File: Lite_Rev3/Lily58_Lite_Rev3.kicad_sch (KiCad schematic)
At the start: 118 parts, among them J1 M2HOLE, J10 LOGO, J10 M2HOLE, J11 LOGO, J11 M2HOLE, J12 HOLE, J13 HOLE, J14 HOLE, J15 HOLE, J16 OLED_R, J19 breakaway, J2 M2HOLE, J20 breakaway, J21 breakaway, J22 AudioJack4, J22 breakaway, J3 HOLE, J4 HOLE, J5 HOLE, J6 HOLE, J7 OLED_L, J9 AudioJack4, SW1 SW_Push, SW10 SW_Push, SW11 SW_Push, SW12 SW_Push, SW13 SW_Push, SW14 SW_Push, SW15 SW_Push, SW16 SW_Push, SW17 SW_Push, SW18 SW_Push, SW19 SW_Push, SW2 SW_Push, SW20 SW_Push, SW21 SW_Push, SW22 SW_Push, SW23 SW_Push, SW24 SW_Push, SW25 SW_Push, SW26 SW_Push, SW27 SW_Push, SW28 SW_Push, SW29 SW_Push, SW3 SW_Push, SW30 SW_Push, SW31 SW_Push, SW32 SW_Push, SW33 SW_Push, SW34 SW_Push, SW35 SW_Push, SW36 SW_Push, SW37 SW_Push, SW38 SW_Push, SW39 SW_Push, SW4 SW_Push, SW40 SW_Push, SW41 SW_Push, SW42 SW_Push, SW43 SW_Push, SW44 SW_Push, SW45 SW_Push, SW46 SW_Push, SW47 SW_Push, SW48 SW_Push, SW49 SW_Push, SW5 SW_Push, SW50 SW_Push, SW51 SW_Push, SW52 SW_Push, SW53 SW_Push, SW54 SW_Push, SW55 SW_Push, SW56 SW_Push, SW57 SW_Push, SW58 SW_Push, SW6 SW_Push, SW7 SW_Push, SW8 SW_Push, SW9 SW_Push

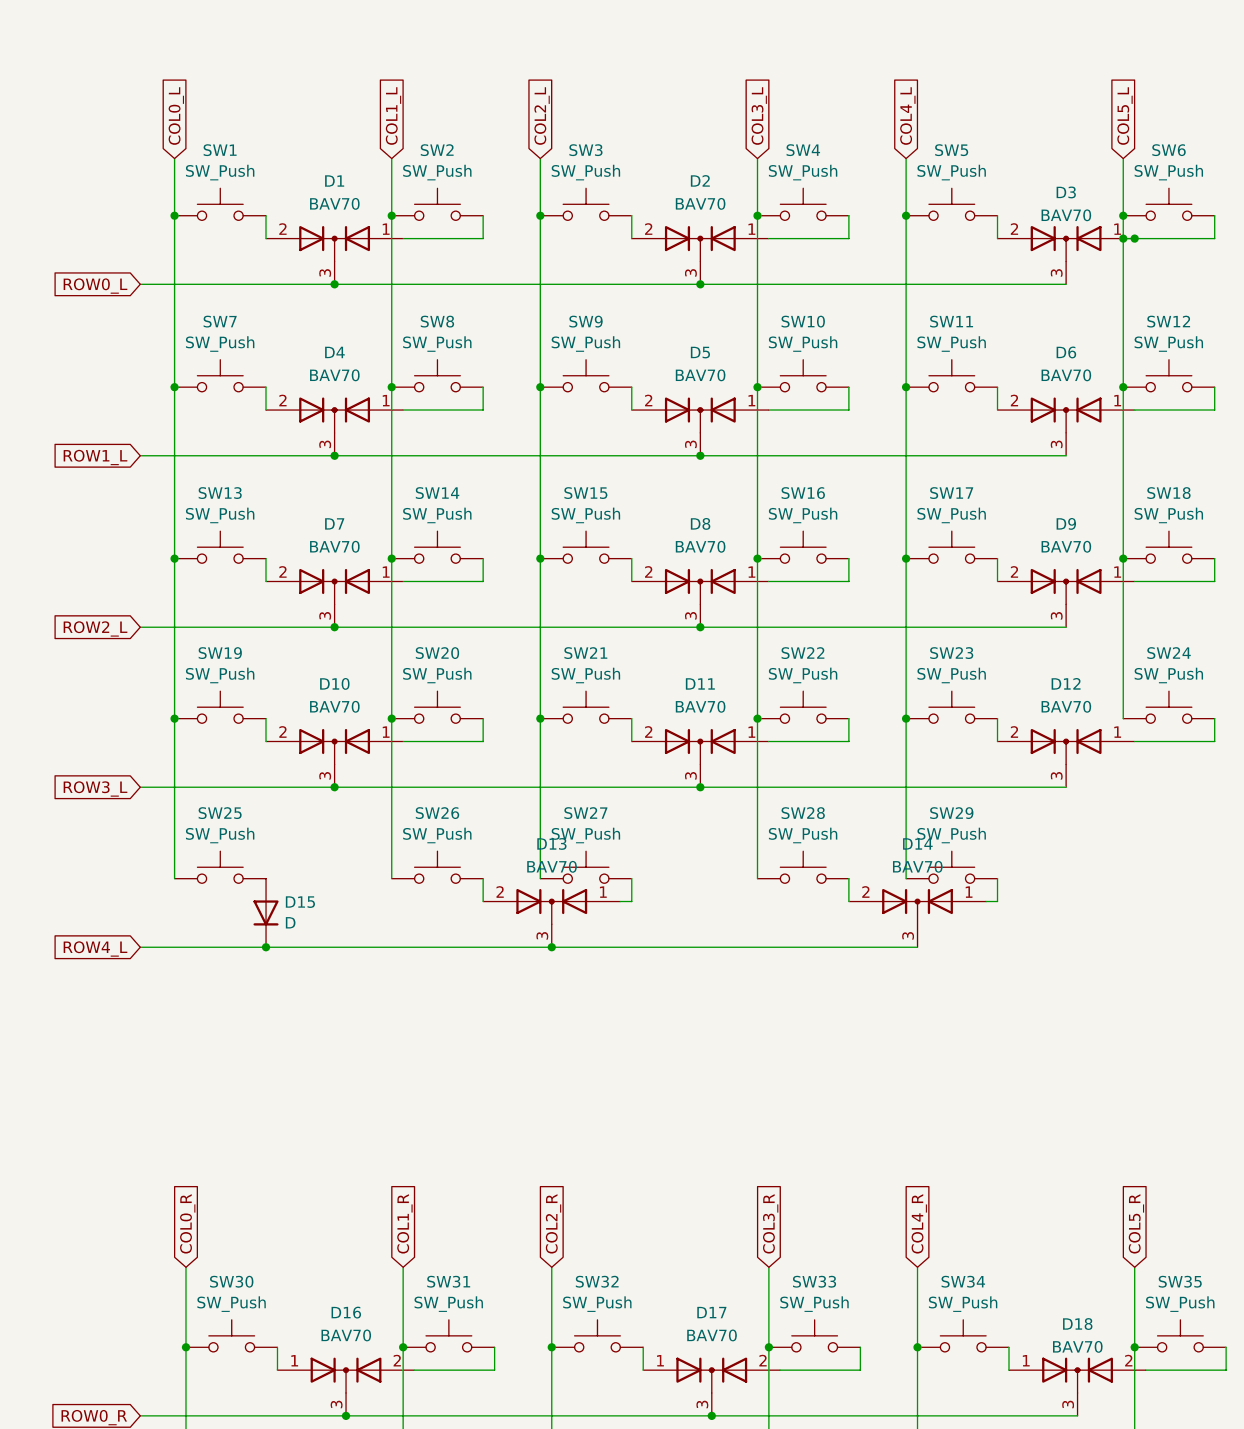
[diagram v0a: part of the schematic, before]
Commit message: [Lily58 Lite Rev3] fix cols pin
Changed to the same cols pin as Lily58 Pro and Lily58 Pro v2
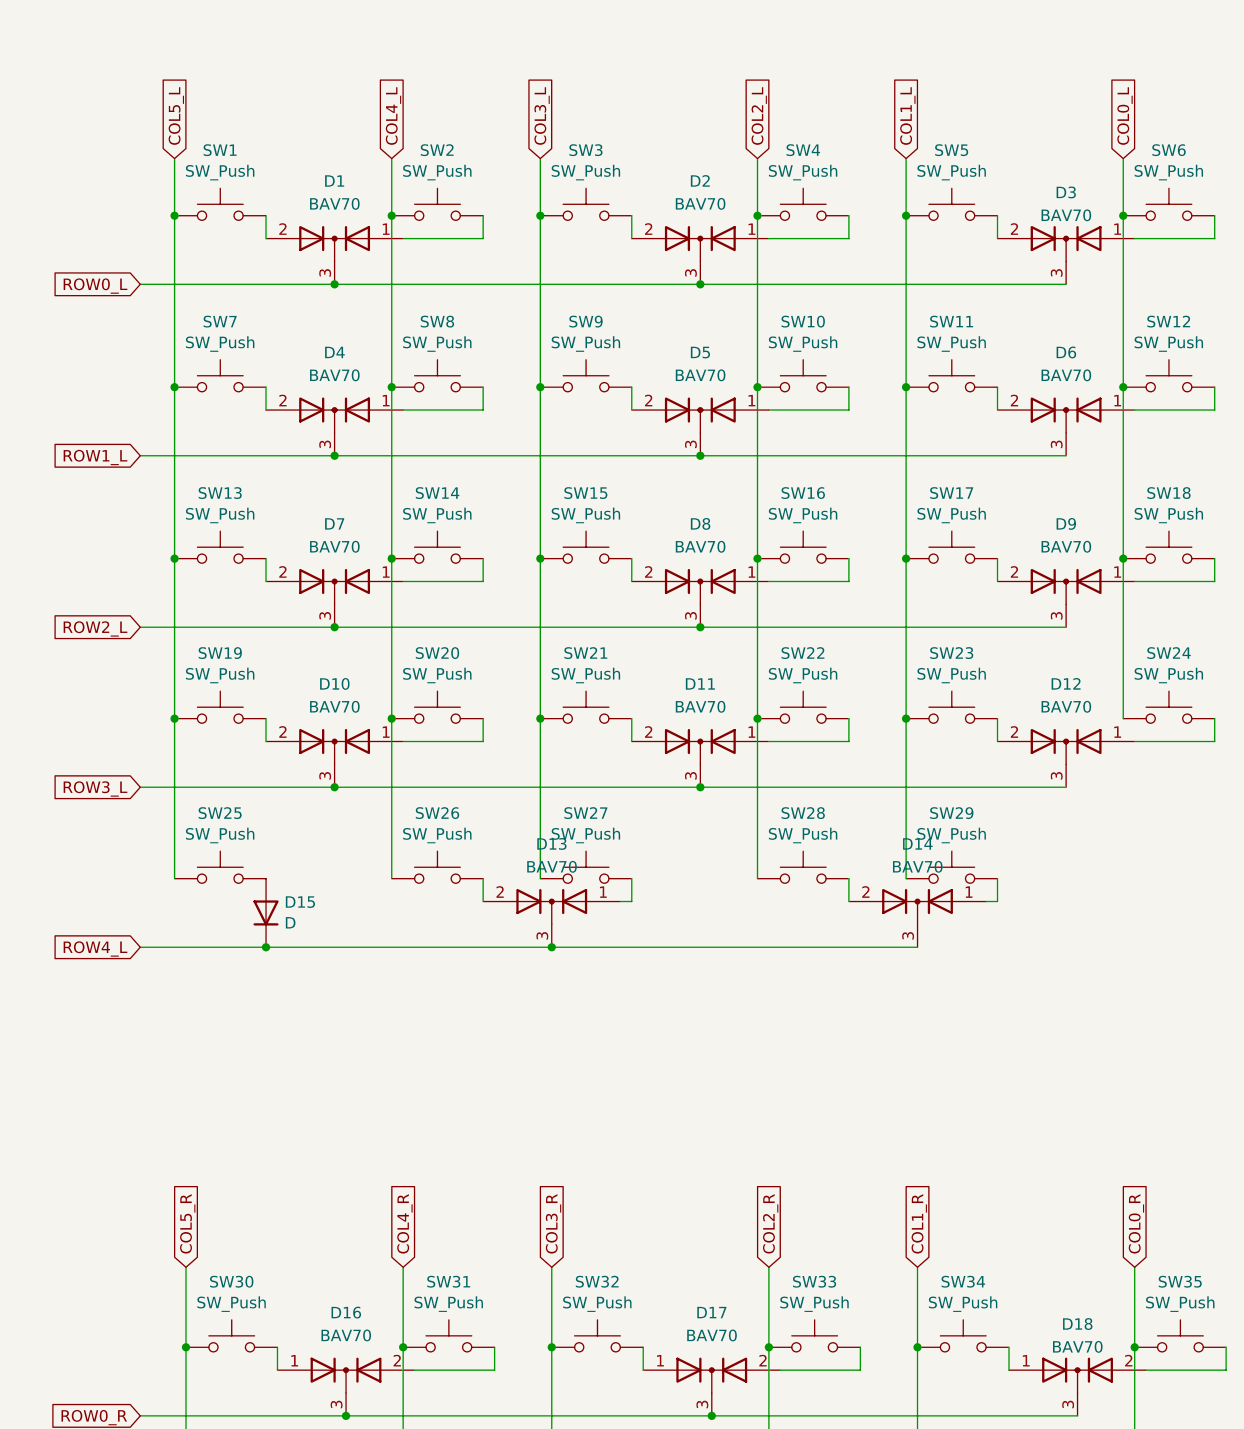
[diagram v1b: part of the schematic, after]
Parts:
- SW1, SW10, SW11, SW12, SW13, SW14, SW15, SW16, SW17, SW18, SW19, SW2, SW20, SW21, SW22, SW23, SW24, SW25, SW26, SW27, SW28, SW29, SW3, SW30, SW31, SW32, SW33, SW34, SW35, SW36, SW37, SW38, SW39, SW4, SW40, SW41, SW42, SW43, SW44, SW45, SW46, SW47, SW48, SW49, SW5, SW50, SW51, SW52, SW53, SW54, SW55, SW56, SW57, SW58, SW6, SW7, SW8, SW9: footprint yuchi_kbd:MX_HOLE -> yuchi:MX_HOLE_FB-SIlk
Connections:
- net COL0_L: now also SW12.1, SW18.1, SW24.1, SW6.1; no longer SW1.1, SW13.1, SW19.1, SW25.1, SW7.1
- net COL0_R: now also SW35.1, SW41.1, SW47.1, SW53.1; no longer SW30.1, SW36.1, SW42.1, SW48.1, SW54.1
- net COL1_L: now also SW11.1, SW17.1, SW23.1, SW29.1, SW5.1; no longer SW14.1, SW2.1, SW20.1, SW26.1, SW8.1
- net COL1_R: now also SW34.1, SW40.1, SW46.1, SW52.1, SW58.1; no longer SW31.1, SW37.1, SW43.1, SW49.1, SW55.1
- net COL2_L: now also SW10.1, SW16.1, SW22.1, SW28.1, SW4.1; no longer SW15.1, SW21.1, SW27.1, SW3.1, SW9.1
- net COL2_R: now also SW33.1, SW39.1, SW45.1, SW51.1, SW57.1; no longer SW32.1, SW38.1, SW44.1, SW50.1, SW56.1
- net COL3_L: now also SW15.1, SW21.1, SW27.1, SW3.1, SW9.1; no longer SW10.1, SW16.1, SW22.1, SW28.1, SW4.1
- net COL3_R: now also SW32.1, SW38.1, SW44.1, SW50.1, SW56.1; no longer SW33.1, SW39.1, SW45.1, SW51.1, SW57.1
- net COL4_L: now also SW14.1, SW2.1, SW20.1, SW26.1, SW8.1; no longer SW11.1, SW17.1, SW23.1, SW29.1, SW5.1
- net COL4_R: now also SW31.1, SW37.1, SW43.1, SW49.1, SW55.1; no longer SW34.1, SW40.1, SW46.1, SW52.1, SW58.1
- net COL5_L: now also SW1.1, SW13.1, SW19.1, SW25.1, SW7.1; no longer D3.1 (A), SW12.1, SW18.1, SW24.1, SW6.1, SW6.2
- net COL5_R: now also SW30.1, SW36.1, SW42.1, SW48.1, SW54.1; no longer SW35.1, SW41.1, SW47.1, SW53.1
- new net: D3.1 (A), SW6.2

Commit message: [Lily58 Lite Rev3] Fix SW54
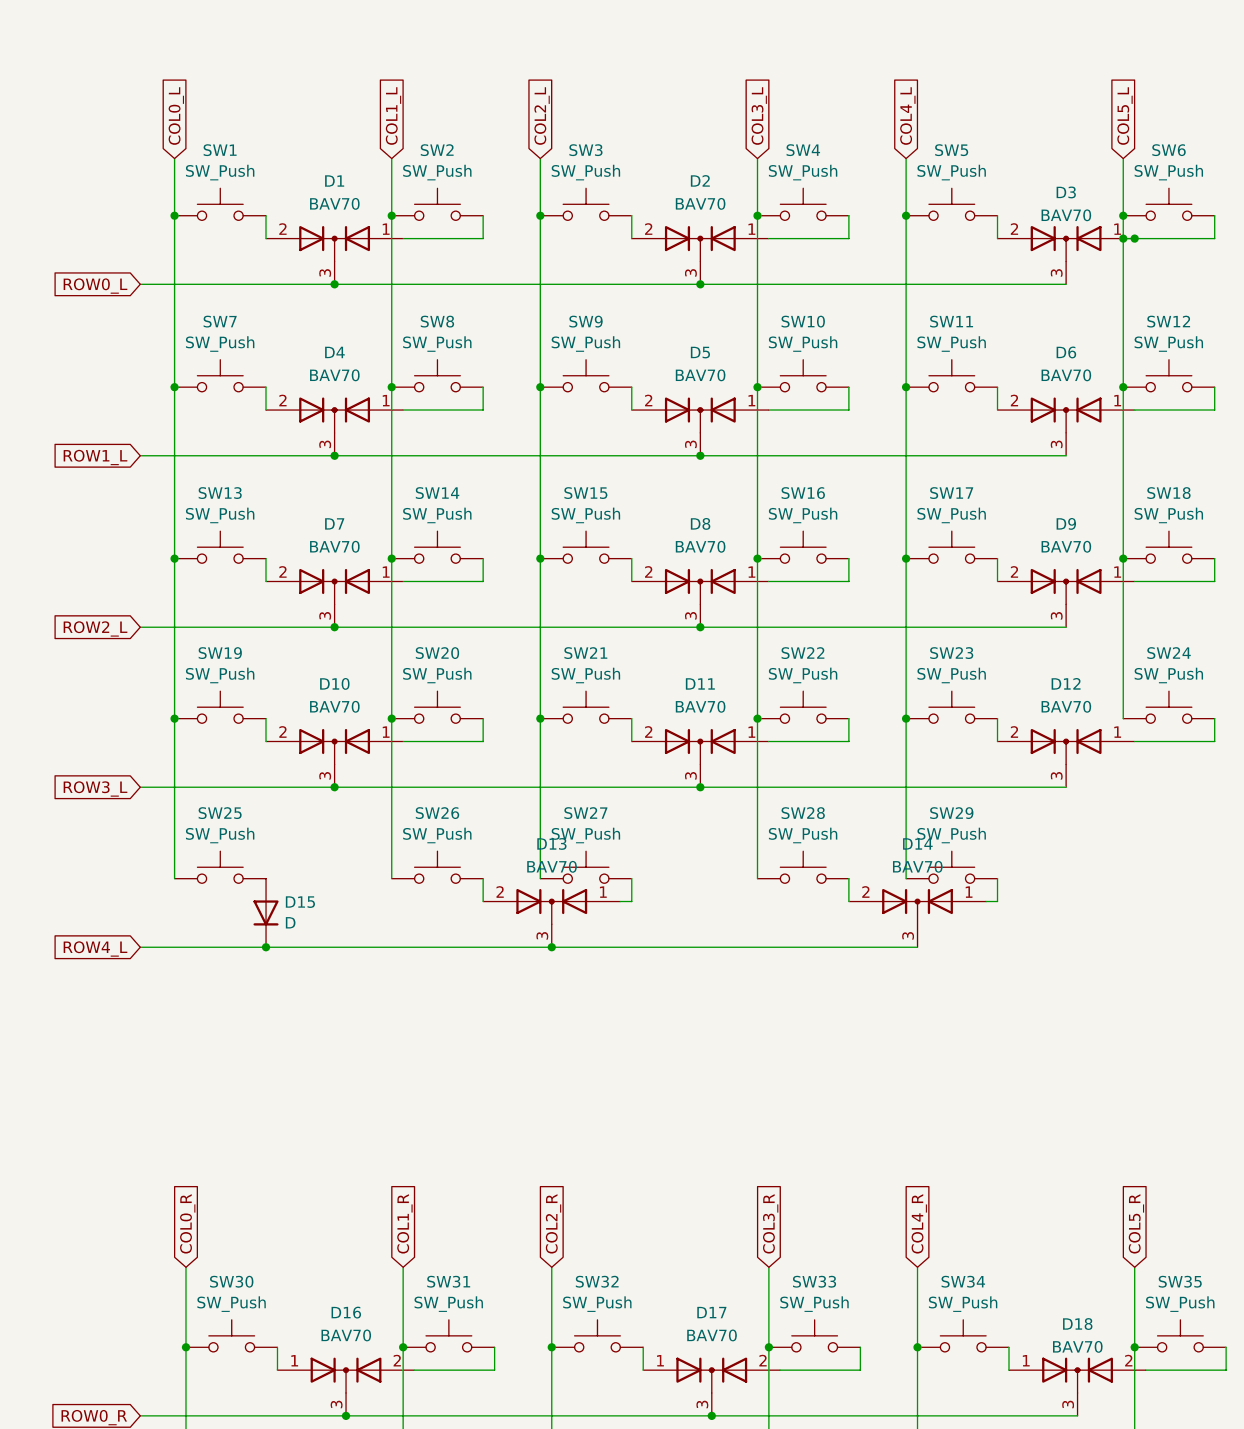
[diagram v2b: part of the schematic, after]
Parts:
- SW1, SW10, SW11, SW12, SW13, SW14, SW15, SW16, SW17, SW18, SW19, SW2, SW20, SW21, SW22, SW23, SW24, SW25, SW26, SW27, SW28, SW29, SW3, SW30, SW31, SW32, SW33, SW34, SW35, SW36, SW37, SW38, SW39, SW4, SW40, SW41, SW42, SW43, SW44, SW45, SW46, SW47, SW48, SW49, SW5, SW50, SW51, SW52, SW53, SW54, SW55, SW56, SW57, SW58, SW6, SW7, SW8, SW9: footprint yuchi:MX_HOLE_FB-SIlk -> yuchi_kbd:MX_HOLE
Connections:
- net COL0_L: now also SW1.1, SW13.1, SW19.1, SW25.1, SW7.1; no longer SW12.1, SW18.1, SW24.1, SW6.1
- net COL0_R: now also SW30.1, SW36.1, SW42.1, SW48.1, SW54.1; no longer SW35.1, SW41.1, SW47.1, SW53.1
- net COL1_L: now also SW14.1, SW2.1, SW20.1, SW26.1, SW8.1; no longer SW11.1, SW17.1, SW23.1, SW29.1, SW5.1
- net COL1_R: now also SW31.1, SW37.1, SW43.1, SW49.1, SW55.1; no longer SW34.1, SW40.1, SW46.1, SW52.1, SW58.1
- net COL2_L: now also SW15.1, SW21.1, SW27.1, SW3.1, SW9.1; no longer SW10.1, SW16.1, SW22.1, SW28.1, SW4.1
- net COL2_R: now also SW32.1, SW38.1, SW44.1, SW50.1, SW56.1; no longer SW33.1, SW39.1, SW45.1, SW51.1, SW57.1
- net COL3_L: now also SW10.1, SW16.1, SW22.1, SW28.1, SW4.1; no longer SW15.1, SW21.1, SW27.1, SW3.1, SW9.1
- net COL3_R: now also SW33.1, SW39.1, SW45.1, SW51.1, SW57.1; no longer SW32.1, SW38.1, SW44.1, SW50.1, SW56.1
- net COL4_L: now also SW11.1, SW17.1, SW23.1, SW29.1, SW5.1; no longer SW14.1, SW2.1, SW20.1, SW26.1, SW8.1
- net COL4_R: now also SW34.1, SW40.1, SW46.1, SW52.1, SW58.1; no longer SW31.1, SW37.1, SW43.1, SW49.1, SW55.1
- net COL5_L: now also D3.1 (A), SW12.1, SW18.1, SW24.1, SW6.1, SW6.2; no longer SW1.1, SW13.1, SW19.1, SW25.1, SW7.1
- net COL5_R: now also SW35.1, SW41.1, SW47.1, SW53.1; no longer SW30.1, SW36.1, SW42.1, SW48.1, SW54.1
